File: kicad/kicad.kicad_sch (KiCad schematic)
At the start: 256 parts, among them J1 USB_B_Micro, J2 SWD, J3 pwr_led+, J4 pwr_led-, J5 caps_led+, J6 caps_led-, U1 AMS1117-3.3, Y1 16MGz, sw1 Esc, sw10 Z, sw100 N5, sw101 N6, sw102 N2, sw103 N1, sw104 N0, sw105 MPlay, sw106 MFwd, sw107 NSlash, sw108 NStar, sw109 N8, sw11 LCtrl, sw110 N9, sw111 NMinus, sw112 NPlus, sw113 NEnter, sw114 N3, sw115 NPeriod, sw12 LSys, sw13 F2, sw14 F3, sw15 2, sw16 3, sw17 W, sw18 E, sw19 S, sw2 F1, sw20 D, sw21 X, sw22 C, sw23 LAlt, sw24 THome, sw25 F4, sw26 F5, sw27 4, sw28 5, sw29 R, sw3 Tilda, sw30 T, sw31 F, sw32 G, sw33 V, sw34 B, sw35 LSpace, sw36 TLeft, sw37 F6, sw38 F7, sw39 6, sw4 1, sw40 7, sw41 Y, sw42 U, sw43 H, sw44 J, sw45 N, sw46 M, sw47 TUp, sw48 TDown, sw49 F8, sw5 Tab, sw50 F9, sw51 8, sw52 9, sw53 I, sw54 O, sw55 K, sw56 L, sw57 Comma, sw58 Period, sw59 RSpace, sw6 Q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

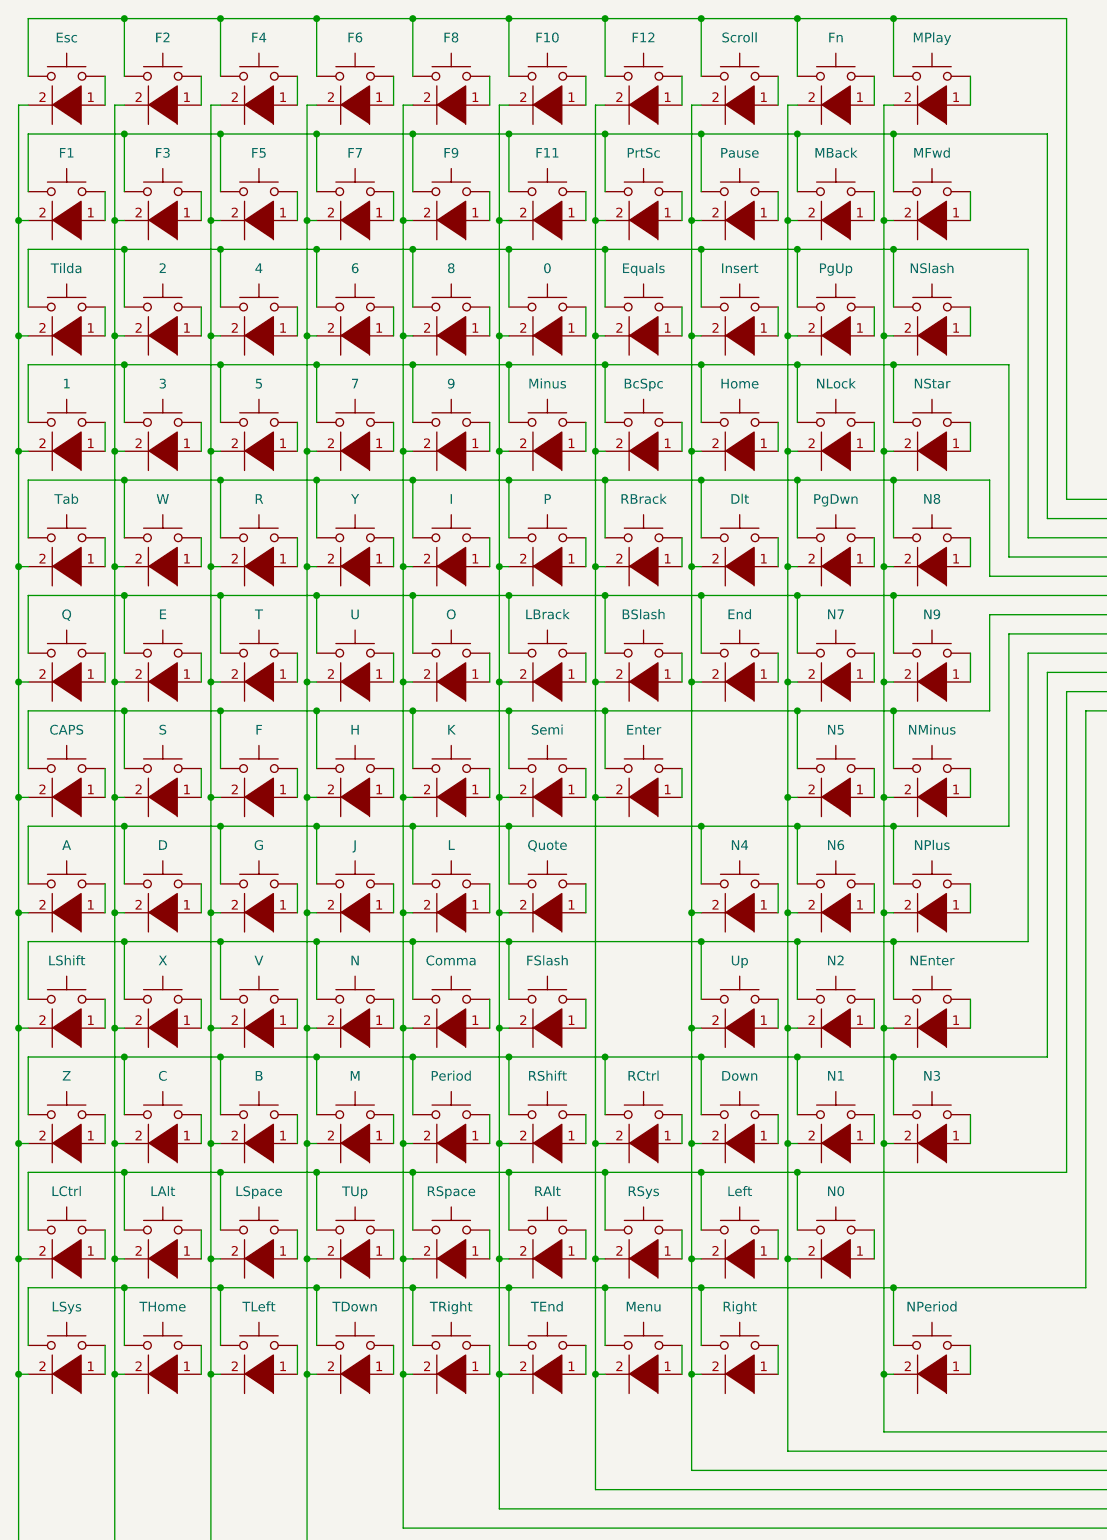
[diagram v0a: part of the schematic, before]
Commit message: layout new diodes
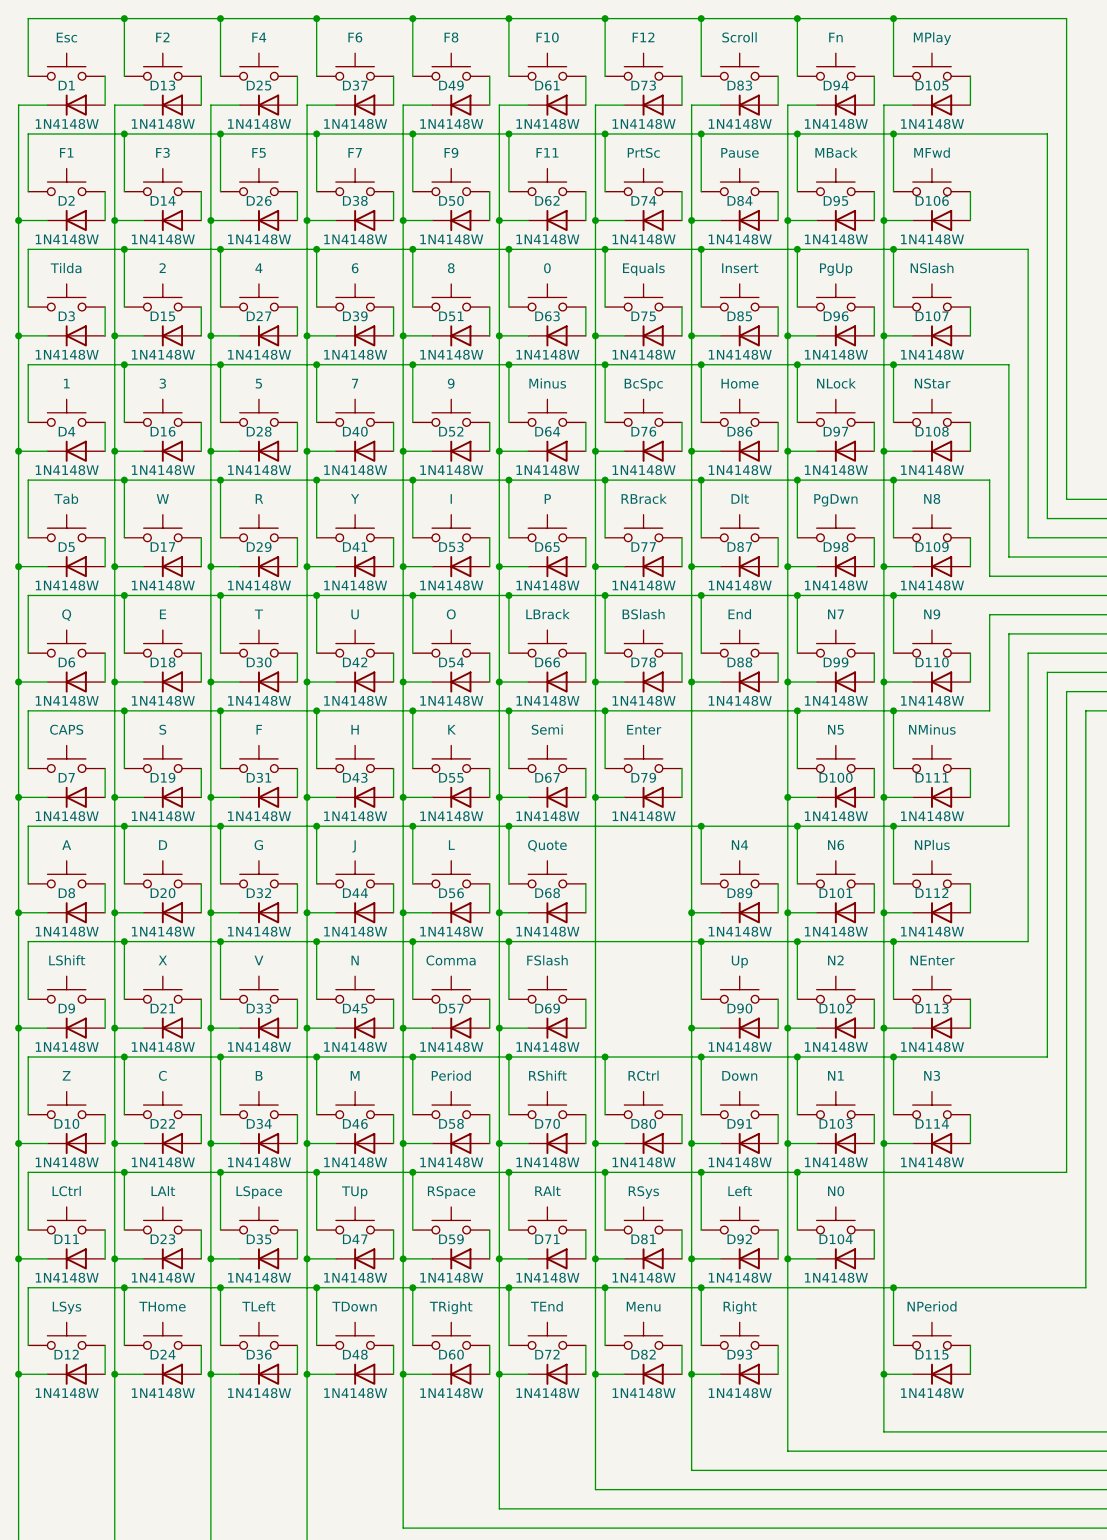
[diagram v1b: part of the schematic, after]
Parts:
- removed D1: D-Esc, Diode_SMD:D_SOD-123F, symbol pspice:DIODE
- removed D10: D-Z, Diode_SMD:D_SOD-123F, symbol pspice:DIODE
- removed D100: D-Num5, Diode_SMD:D_SOD-123F, symbol pspice:DIODE
- removed D101: D-Num6, Diode_SMD:D_SOD-123F, symbol pspice:DIODE
- removed D102: D-Num2, Diode_SMD:D_SOD-123F, symbol pspice:DIODE
- removed D103: D-Num1, Diode_SMD:D_SOD-123F, symbol pspice:DIODE
- removed D104: D-Num0, Diode_SMD:D_SOD-123F, symbol pspice:DIODE
- removed D105: D-mPlay, Diode_SMD:D_SOD-123F, symbol pspice:DIODE
- removed D106: D-mFwd, Diode_SMD:D_SOD-123F, symbol pspice:DIODE
- removed D107: D-Num/, Diode_SMD:D_SOD-123F, symbol pspice:DIODE
- removed D108: D-Num*, Diode_SMD:D_SOD-123F, symbol pspice:DIODE
- removed D109: D-Num8, Diode_SMD:D_SOD-123F, symbol pspice:DIODE
- removed D11: D-LCtrl, Diode_SMD:D_SOD-123F, symbol pspice:DIODE
- removed D110, D99: D-Num9, Diode_SMD:D_SOD-123F, symbol pspice:DIODE
- removed D111: D-Num-, Diode_SMD:D_SOD-123F, symbol pspice:DIODE
- removed D112: D-Num+, Diode_SMD:D_SOD-123F, symbol pspice:DIODE
- removed D113: D-NumEnter, Diode_SMD:D_SOD-123F, symbol pspice:DIODE
- removed D114: D-Num3, Diode_SMD:D_SOD-123F, symbol pspice:DIODE
- removed D115: D-Num., Diode_SMD:D_SOD-123F, symbol pspice:DIODE
- removed D12: D-LSys, Diode_SMD:D_SOD-123F, symbol pspice:DIODE
- removed D13: D-F2, Diode_SMD:D_SOD-123F, symbol pspice:DIODE
- removed D14: D-F3, Diode_SMD:D_SOD-123F, symbol pspice:DIODE
- removed D15: D-2, Diode_SMD:D_SOD-123F, symbol pspice:DIODE
- removed D16: D-3, Diode_SMD:D_SOD-123F, symbol pspice:DIODE
- removed D17: D-W, Diode_SMD:D_SOD-123F, symbol pspice:DIODE
- removed D18: D-E, Diode_SMD:D_SOD-123F, symbol pspice:DIODE
- removed D19: D-S, Diode_SMD:D_SOD-123F, symbol pspice:DIODE
- removed D2: D-F1, Diode_SMD:D_SOD-123F, symbol pspice:DIODE
- removed D20: D-D, Diode_SMD:D_SOD-123F, symbol pspice:DIODE
- removed D21: D-X, Diode_SMD:D_SOD-123F, symbol pspice:DIODE
- removed D22: D-C, Diode_SMD:D_SOD-123F, symbol pspice:DIODE
- removed D23: D-LAlt, Diode_SMD:D_SOD-123F, symbol pspice:DIODE
- removed D24: D-THome, Diode_SMD:D_SOD-123F, symbol pspice:DIODE
- removed D25: D-F4, Diode_SMD:D_SOD-123F, symbol pspice:DIODE
- removed D26: D-F5, Diode_SMD:D_SOD-123F, symbol pspice:DIODE
- removed D27: D-4, Diode_SMD:D_SOD-123F, symbol pspice:DIODE
- removed D28: D-5, Diode_SMD:D_SOD-123F, symbol pspice:DIODE
- removed D29: D-R, Diode_SMD:D_SOD-123F, symbol pspice:DIODE
- removed D3: D-Tilda, Diode_SMD:D_SOD-123F, symbol pspice:DIODE
- removed D30: D-T, Diode_SMD:D_SOD-123F, symbol pspice:DIODE
- removed D31: D-F, Diode_SMD:D_SOD-123F, symbol pspice:DIODE
- removed D32: D-G, Diode_SMD:D_SOD-123F, symbol pspice:DIODE
- removed D33: D-V, Diode_SMD:D_SOD-123F, symbol pspice:DIODE
- removed D34: D-B, Diode_SMD:D_SOD-123F, symbol pspice:DIODE
- removed D35: D-LSpace, Diode_SMD:D_SOD-123F, symbol pspice:DIODE
- removed D36: D-TLeft, Diode_SMD:D_SOD-123F, symbol pspice:DIODE
- removed D37: D-F6, Diode_SMD:D_SOD-123F, symbol pspice:DIODE
- removed D38: D-F7, Diode_SMD:D_SOD-123F, symbol pspice:DIODE
- removed D39: D-6, Diode_SMD:D_SOD-123F, symbol pspice:DIODE
- removed D4: D-1, Diode_SMD:D_SOD-123F, symbol pspice:DIODE
- removed D40: D-7, Diode_SMD:D_SOD-123F, symbol pspice:DIODE
- removed D41: D-Y, Diode_SMD:D_SOD-123F, symbol pspice:DIODE
- removed D42: D-U, Diode_SMD:D_SOD-123F, symbol pspice:DIODE
- removed D43: D-H, Diode_SMD:D_SOD-123F, symbol pspice:DIODE
- removed D44: D-J, Diode_SMD:D_SOD-123F, symbol pspice:DIODE
- removed D45: D-N, Diode_SMD:D_SOD-123F, symbol pspice:DIODE
- removed D46: D-M, Diode_SMD:D_SOD-123F, symbol pspice:DIODE
- removed D47: D-TUp, Diode_SMD:D_SOD-123F, symbol pspice:DIODE
- removed D48: D-TDown, Diode_SMD:D_SOD-123F, symbol pspice:DIODE
- removed D49: D-F8, Diode_SMD:D_SOD-123F, symbol pspice:DIODE
- removed D5: D-Tab, Diode_SMD:D_SOD-123F, symbol pspice:DIODE
- removed D50: D-F9, Diode_SMD:D_SOD-123F, symbol pspice:DIODE
- removed D51: D-8, Diode_SMD:D_SOD-123F, symbol pspice:DIODE
- removed D52: D-9, Diode_SMD:D_SOD-123F, symbol pspice:DIODE
- removed D53: D-I, Diode_SMD:D_SOD-123F, symbol pspice:DIODE
- removed D54: D-O, Diode_SMD:D_SOD-123F, symbol pspice:DIODE
- removed D55: D-K, Diode_SMD:D_SOD-123F, symbol pspice:DIODE
- removed D56: D-L, Diode_SMD:D_SOD-123F, symbol pspice:DIODE
- removed D57: D-,, Diode_SMD:D_SOD-123F, symbol pspice:DIODE
- removed D58: D-., Diode_SMD:D_SOD-123F, symbol pspice:DIODE
- removed D59: D-RSpace, Diode_SMD:D_SOD-123F, symbol pspice:DIODE
- removed D6: D-Q, Diode_SMD:D_SOD-123F, symbol pspice:DIODE
- removed D60: D-TRight, Diode_SMD:D_SOD-123F, symbol pspice:DIODE
- removed D61: D-F10, Diode_SMD:D_SOD-123F, symbol pspice:DIODE
- removed D62: D-F11, Diode_SMD:D_SOD-123F, symbol pspice:DIODE
- removed D63: D-0, Diode_SMD:D_SOD-123F, symbol pspice:DIODE
- removed D64: D--, Diode_SMD:D_SOD-123F, symbol pspice:DIODE
- removed D65: D-P, Diode_SMD:D_SOD-123F, symbol pspice:DIODE
- removed D66: D-[, Diode_SMD:D_SOD-123F, symbol pspice:DIODE
- removed D67: D-;, Diode_SMD:D_SOD-123F, symbol pspice:DIODE
- removed D68: D-', Diode_SMD:D_SOD-123F, symbol pspice:DIODE
- removed D69: D-/, Diode_SMD:D_SOD-123F, symbol pspice:DIODE
- removed D7: D-CAPS, Diode_SMD:D_SOD-123F, symbol pspice:DIODE
- removed D70: D-RShift, Diode_SMD:D_SOD-123F, symbol pspice:DIODE
- removed D71: D-RAlt, Diode_SMD:D_SOD-123F, symbol pspice:DIODE
- removed D72: D-TEnd, Diode_SMD:D_SOD-123F, symbol pspice:DIODE
- removed D73: D-F12, Diode_SMD:D_SOD-123F, symbol pspice:DIODE
- removed D74: D-PrtSc, Diode_SMD:D_SOD-123F, symbol pspice:DIODE
- removed D75: D-=, Diode_SMD:D_SOD-123F, symbol pspice:DIODE
- removed D76: D-BcSpc, Diode_SMD:D_SOD-123F, symbol pspice:DIODE
- removed D77: D-], Diode_SMD:D_SOD-123F, symbol pspice:DIODE
- removed D78: D-\, Diode_SMD:D_SOD-123F, symbol pspice:DIODE
- removed D79: D-Enter, Diode_SMD:D_SOD-123F, symbol pspice:DIODE
- removed D8: D-A, Diode_SMD:D_SOD-123F, symbol pspice:DIODE
- removed D80: D-RCtrl, Diode_SMD:D_SOD-123F, symbol pspice:DIODE
- removed D81: D-RSys, Diode_SMD:D_SOD-123F, symbol pspice:DIODE
- removed D82: D-Menu, Diode_SMD:D_SOD-123F, symbol pspice:DIODE
- removed D83: D-ScrLck, Diode_SMD:D_SOD-123F, symbol pspice:DIODE
- removed D84: D-Pause, Diode_SMD:D_SOD-123F, symbol pspice:DIODE
- removed D85: D-Insert, Diode_SMD:D_SOD-123F, symbol pspice:DIODE
- removed D86: D-Home, Diode_SMD:D_SOD-123F, symbol pspice:DIODE
- removed D87: D-Dlt, Diode_SMD:D_SOD-123F, symbol pspice:DIODE
- removed D88: D-End, Diode_SMD:D_SOD-123F, symbol pspice:DIODE
- removed D89: D-Num4, Diode_SMD:D_SOD-123F, symbol pspice:DIODE
- removed D9: D-LShift, Diode_SMD:D_SOD-123F, symbol pspice:DIODE
- removed D90: D-Up, Diode_SMD:D_SOD-123F, symbol pspice:DIODE
- removed D91: D-Down, Diode_SMD:D_SOD-123F, symbol pspice:DIODE
- removed D92: D-Left, Diode_SMD:D_SOD-123F, symbol pspice:DIODE
- removed D93: D-Right, Diode_SMD:D_SOD-123F, symbol pspice:DIODE
- removed D94: D-FN, Diode_SMD:D_SOD-123F, symbol pspice:DIODE
- removed D95: D-mBack, Diode_SMD:D_SOD-123F, symbol pspice:DIODE
- removed D96: D-PgUp, Diode_SMD:D_SOD-123F, symbol pspice:DIODE
- removed D97: D-NumLck, Diode_SMD:D_SOD-123F, symbol pspice:DIODE
- removed D98: D-PgDwn, Diode_SMD:D_SOD-123F, symbol pspice:DIODE
- added D1, D10, D100, D101, D102, D103, D104, D105, D106, D107, D108, D109, D11, D110, D111, D112, D113, D114, D115, D12, D13, D14, D15, D16, D17, D18, D19, D2, D20, D21, D22, D23, D24, D25, D26, D27, D28, D29, D3, D30, D31, D32, D33, D34, D35, D36, D37, D38, D39, D4, D40, D41, D42, D43, D44, D45, D46, D47, D48, D49, D5, D50, D51, D52, D53, D54, D55, D56, D57, D58, D59, D6, D60, D61, D62, D63, D64, D65, D66, D67, D68, D69, D7, D70, D71, D72, D73, D74, D75, D76, D77, D78, D79, D8, D80, D81, D82, D83, D84, D85, D86, D87, D88, D89, D9, D90, D91, D92, D93, D94, D95, D96, D97, D98, D99: 1N4148W, Diode_SMD:D_SOD-123, symbol Diode:1N4148W
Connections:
- net COLUMN1: now also D105.1 (K), D106.1 (K), D107.1 (K), D108.1 (K), D109.1 (K), D110.1 (K), D111.1 (K), D112.1 (K), D113.1 (K), D114.1 (K), D115.1 (K)
- net COLUMN10: now also D1.1 (K), D10.1 (K), D11.1 (K), D12.1 (K), D2.1 (K), D3.1 (K), D4.1 (K), D5.1 (K), D6.1 (K), D7.1 (K), D8.1 (K), D9.1 (K)
- net COLUMN2: now also D100.1 (K), D101.1 (K), D102.1 (K), D103.1 (K), D104.1 (K), D94.1 (K), D95.1 (K), D96.1 (K), D97.1 (K), D98.1 (K), D99.1 (K)
- net COLUMN3: now also D83.1 (K), D84.1 (K), D85.1 (K), D86.1 (K), D87.1 (K), D88.1 (K), D89.1 (K), D90.1 (K), D91.1 (K), D92.1 (K), D93.1 (K)
- net COLUMN4: now also D73.1 (K), D74.1 (K), D75.1 (K), D76.1 (K), D77.1 (K), D78.1 (K), D79.1 (K), D80.1 (K), D81.1 (K), D82.1 (K)
- net COLUMN5: now also D61.1 (K), D62.1 (K), D63.1 (K), D64.1 (K), D65.1 (K), D66.1 (K), D67.1 (K), D68.1 (K), D69.1 (K), D70.1 (K), D71.1 (K), D72.1 (K)
- net COLUMN6: now also D49.1 (K), D50.1 (K), D51.1 (K), D52.1 (K), D53.1 (K), D54.1 (K), D55.1 (K), D56.1 (K), D57.1 (K), D58.1 (K), D59.1 (K), D60.1 (K)
- net COLUMN7: now also D37.1 (K), D38.1 (K), D39.1 (K), D40.1 (K), D41.1 (K), D42.1 (K), D43.1 (K), D44.1 (K), D45.1 (K), D46.1 (K), D47.1 (K), D48.1 (K)
- net COLUMN8: now also D25.1 (K), D26.1 (K), D27.1 (K), D28.1 (K), D29.1 (K), D30.1 (K), D31.1 (K), D32.1 (K), D33.1 (K), D34.1 (K), D35.1 (K), D36.1 (K)
- net COLUMN9: now also D13.1 (K), D14.1 (K), D15.1 (K), D16.1 (K), D17.1 (K), D18.1 (K), D19.1 (K), D20.1 (K), D21.1 (K), D22.1 (K), D23.1 (K), D24.1 (K)
- net at sw17.2: now also D17.2 (A)
- net at sw104.2: now also D104.2 (A)
- net at sw38.2: now also D38.2 (A)
- net at sw59.2: now also D59.2 (A)
- net at sw1.2: now also D1.2 (A)
- net at sw19.2: now also D19.2 (A)
- net at sw70.2: now also D70.2 (A)
- net at sw102.2: now also D102.2 (A)
- net at sw47.2: now also D47.2 (A)
- net at sw92.2: now also D92.2 (A)
- net at sw48.2: now also D48.2 (A)
- net at sw72.2: now also D72.2 (A)
- net at sw34.2: now also D34.2 (A)
- net at sw40.2: now also D40.2 (A)
- net at sw99.2: now also D99.2 (A)
- net at sw24.2: now also D24.2 (A)
- net at sw12.2: now also D12.2 (A)
- net at sw80.2: now also D80.2 (A)
- net at sw113.2: now also D113.2 (A)
- net at sw91.2: now also D91.2 (A)
- net at sw63.2: now also D63.2 (A)
- net at sw100.2: now also D100.2 (A)
- net at sw36.2: now also D36.2 (A)
- net at sw53.2: now also D53.2 (A)
- net at sw106.2: now also D106.2 (A)
- net at sw27.2: now also D27.2 (A)
- net at sw60.2: now also D60.2 (A)
- net at sw8.2: now also D8.2 (A)
- net at sw9.2: now also D9.2 (A)
- net at sw58.2: now also D58.2 (A)
- net at sw98.2: now also D98.2 (A)
- net at sw51.2: now also D51.2 (A)
- net at sw7.2: now also D7.2 (A)
- net at sw20.2: now also D20.2 (A)
- net at sw22.2: now also D22.2 (A)
- net at sw28.2: now also D28.2 (A)
- net at sw35.2: now also D35.2 (A)
- net at sw84.2: now also D84.2 (A)
- net at sw13.2: now also D13.2 (A)
- net at sw97.2: now also D97.2 (A)
- net at sw71.2: now also D71.2 (A)
- net at sw61.2: now also D61.2 (A)
- net at sw50.2: now also D50.2 (A)
- net at sw86.2: now also D86.2 (A)
- net at sw109.2: now also D109.2 (A)
- net at sw41.2: now also D41.2 (A)
- net at sw85.2: now also D85.2 (A)
- net at sw31.2: now also D31.2 (A)
- net at sw93.2: now also D93.2 (A)
- net at sw16.2: now also D16.2 (A)
- net at sw75.2: now also D75.2 (A)
- net at sw78.2: now also D78.2 (A)
- net at sw26.2: now also D26.2 (A)
- net at sw21.2: now also D21.2 (A)
- net at sw89.2: now also D89.2 (A)
- net at sw74.2: now also D74.2 (A)
- net at sw25.2: now also D25.2 (A)
- net at sw103.2: now also D103.2 (A)
- net at sw114.2: now also D114.2 (A)
- net at sw29.2: now also D29.2 (A)
- net at sw14.2: now also D14.2 (A)
- net at sw73.2: now also D73.2 (A)
- net at sw105.2: now also D105.2 (A)
- net at sw6.2: now also D6.2 (A)
- net at sw55.2: now also D55.2 (A)
- net at sw67.2: now also D67.2 (A)
- net at sw87.2: now also D87.2 (A)
- net at sw69.2: now also D69.2 (A)
- net at sw45.2: now also D45.2 (A)
- net at sw54.2: now also D54.2 (A)
- net at sw77.2: now also D77.2 (A)
- net at sw23.2: now also D23.2 (A)
- net at sw79.2: now also D79.2 (A)
- net at sw66.2: now also D66.2 (A)
- net at sw18.2: now also D18.2 (A)
- net at sw64.2: now also D64.2 (A)
- net at sw52.2: now also D52.2 (A)
- net at sw96.2: now also D96.2 (A)
- net at sw10.2: now also D10.2 (A)
- net at sw111.2: now also D111.2 (A)
- net at sw5.2: now also D5.2 (A)
- net at sw46.2: now also D46.2 (A)
- net at sw4.2: now also D4.2 (A)
- net at sw107.2: now also D107.2 (A)
- net at sw62.2: now also D62.2 (A)
- net at sw88.2: now also D88.2 (A)
- net at sw33.2: now also D33.2 (A)
- net at sw43.2: now also D43.2 (A)
- net at sw108.2: now also D108.2 (A)
- net at sw90.2: now also D90.2 (A)
- net at sw112.2: now also D112.2 (A)
- net at sw95.2: now also D95.2 (A)
- net at sw68.2: now also D68.2 (A)
- net at sw76.2: now also D76.2 (A)
- net at sw94.2: now also D94.2 (A)
- net at sw44.2: now also D44.2 (A)
- net at sw49.2: now also D49.2 (A)
- net at sw115.2: now also D115.2 (A)
- net at sw30.2: now also D30.2 (A)
- net at sw2.2: now also D2.2 (A)
- net at sw42.2: now also D42.2 (A)
- net at sw39.2: now also D39.2 (A)
- net at sw82.2: now also D82.2 (A)
- net at sw56.2: now also D56.2 (A)
- net at sw37.2: now also D37.2 (A)
- net at sw81.2: now also D81.2 (A)
- net at sw65.2: now also D65.2 (A)
- net at sw15.2: now also D15.2 (A)
- net at sw11.2: now also D11.2 (A)
- net at sw57.2: now also D57.2 (A)
- net at sw3.2: now also D3.2 (A)
- net at sw101.2: now also D101.2 (A)
- net at sw110.2: now also D110.2 (A)
- net at sw83.2: now also D83.2 (A)
- net at sw32.2: now also D32.2 (A)

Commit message: correct RShift footprint
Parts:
- sw70: footprint Button_Switch_Keyboard:SW_Cherry_MX_1.00u_PCB -> Button_Switch_Keyboard:SW_Cherry_MX_2.75u_PCB
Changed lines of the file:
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@@
     )
     (property "Value" "RShift" (id 1) (at 105.41 172.72 0))
-    (property "Footprint" "Button_Switch_Keyboard:SW_Cherry_MX_1.00u_PCB" (id 2) (at 105.41 172.72 0)
+    (property "Footprint" "Button_Switch_Keyboard:SW_Cherry_MX_2.75u_PCB" (id 2) (at 105.41 172.72 0)
       (effects (font (size 1.27 1.27)) hide)
     )
@@
     )
     (path "/0a2fbe5c-c0e6-4b3a-854e-12d87ec302d2"
-      (reference "sw70") (unit 1) (value "RShift") (footprint "Button_Switch_Keyboard:SW_Cherry_MX_1.00u_PCB")
+      (reference "sw70") (unit 1) (value "RShift") (footprint "Button_Switch_Keyboard:SW_Cherry_MX_2.75u_PCB")
     )
     (path "/35cfa04a-c5c4-4d67-bfb5-7569bc2b66f1"

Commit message: 75% layout
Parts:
- removed D100, D101, D102, D103, D104, D105, D106, D107, D108, D109, D110, D111, D112, D113, D114, D115, D83, D84, D86, D88, D89, D90, D91, D92, D93, D94, D95, D97, D99: 1N4148W, Diode_SMD:D_SOD-123, symbol Diode:1N4148W
- removed sw100: N5, Button_Switch_Keyboard:SW_Cherry_MX_1.00u_PCB, symbol Switch:SW_Push
- removed sw101: N6, Button_Switch_Keyboard:SW_Cherry_MX_1.00u_PCB, symbol Switch:SW_Push
- removed sw102: N2, Button_Switch_Keyboard:SW_Cherry_MX_1.00u_PCB, symbol Switch:SW_Push
- removed sw103: N1, Button_Switch_Keyboard:SW_Cherry_MX_1.00u_PCB, symbol Switch:SW_Push
- removed sw104: N0, Button_Switch_Keyboard:SW_Cherry_MX_2.00u_PCB, symbol Switch:SW_Push
- removed sw105: MPlay, Button_Switch_Keyboard:SW_Cherry_MX_1.00u_PCB, symbol Switch:SW_Push
- removed sw106: MFwd, Button_Switch_Keyboard:SW_Cherry_MX_1.00u_PCB, symbol Switch:SW_Push
- removed sw107: NSlash, Button_Switch_Keyboard:SW_Cherry_MX_1.00u_PCB, symbol Switch:SW_Push
- removed sw108: NStar, Button_Switch_Keyboard:SW_Cherry_MX_1.00u_PCB, symbol Switch:SW_Push
- removed sw109: N8, Button_Switch_Keyboard:SW_Cherry_MX_1.00u_PCB, symbol Switch:SW_Push
- removed sw110: N9, Button_Switch_Keyboard:SW_Cherry_MX_1.00u_PCB, symbol Switch:SW_Push
- removed sw111: NMinus, Button_Switch_Keyboard:SW_Cherry_MX_1.00u_PCB, symbol Switch:SW_Push
- removed sw112: NPlus, Button_Switch_Keyboard:SW_Cherry_MX_2.00u_Vertical_PCB, symbol Switch:SW_Push
- removed sw113: NEnter, Button_Switch_Keyboard:SW_Cherry_MX_2.00u_Vertical_PCB, symbol Switch:SW_Push
- removed sw114: N3, Button_Switch_Keyboard:SW_Cherry_MX_1.00u_PCB, symbol Switch:SW_Push
- removed sw115: NPeriod, Button_Switch_Keyboard:SW_Cherry_MX_1.00u_PCB, symbol Switch:SW_Push
- removed sw83: Scroll, Button_Switch_Keyboard:SW_Cherry_MX_1.00u_PCB, symbol Switch:SW_Push
- removed sw84: Pause, Button_Switch_Keyboard:SW_Cherry_MX_1.00u_PCB, symbol Switch:SW_Push
- removed sw86: Home, Button_Switch_Keyboard:SW_Cherry_MX_1.00u_PCB, symbol Switch:SW_Push
- removed sw88: End, Button_Switch_Keyboard:SW_Cherry_MX_1.00u_PCB, symbol Switch:SW_Push
- removed sw89: N4, Button_Switch_Keyboard:SW_Cherry_MX_1.00u_PCB, symbol Switch:SW_Push
- removed sw90: Up, Button_Switch_Keyboard:SW_Cherry_MX_1.00u_PCB, symbol Switch:SW_Push
- removed sw91: Down, Button_Switch_Keyboard:SW_Cherry_MX_1.00u_PCB, symbol Switch:SW_Push
- removed sw92: Left, Button_Switch_Keyboard:SW_Cherry_MX_1.00u_PCB, symbol Switch:SW_Push
- removed sw93: Right, Button_Switch_Keyboard:SW_Cherry_MX_1.00u_PCB, symbol Switch:SW_Push
- removed sw94: Fn, Button_Switch_Keyboard:SW_Cherry_MX_1.00u_PCB, symbol Switch:SW_Push
- removed sw95: MBack, Button_Switch_Keyboard:SW_Cherry_MX_1.00u_PCB, symbol Switch:SW_Push
- removed sw97: NLock, Button_Switch_Keyboard:SW_Cherry_MX_1.00u_PCB, symbol Switch:SW_Push
- removed sw99: N7, Button_Switch_Keyboard:SW_Cherry_MX_1.00u_PCB, symbol Switch:SW_Push
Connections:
- net COLUMN1: now also D1.1 (K), D11.1 (K), D3.1 (K), D5.1 (K), D7.1 (K), D9.1 (K)
- net COLUMN10: now also D49.1 (K), D52.1 (K), D54.1 (K), D56.1 (K), D58.1 (K), D71.1 (K); no longer D1.1 (K), D10.1 (K), D11.1 (K), D12.1 (K), D2.1 (K), D3.1 (K), D4.1 (K), D5.1 (K), D6.1 (K), D7.1 (K), D8.1 (K), D9.1 (K)
- net COLUMN2: now also MCU1.39 (PC8), sw15.1, sw16.1, sw27.1, sw28.1, sw3.1, sw39.1, sw4.1, sw40.1, sw51.1, sw52.1, sw63.1, sw64.1, sw75.1, sw76.1; no longer D96.1 (K), D98.1 (K)
- net COLUMN3: now also D15.1 (K), D17.1 (K), D19.1 (K), D2.1 (K), D21.1 (K), D23.1 (K), D96.1 (K); no longer D85.1 (K), D87.1 (K)
- net COLUMN4: now also D13.1 (K), D16.1 (K), D18.1 (K), D20.1 (K), D22.1 (K), D24.1 (K), D35.1 (K); no longer D73.1 (K), D74.1 (K), D75.1 (K), D76.1 (K), D77.1 (K), D78.1 (K), D79.1 (K), D80.1 (K), D81.1 (K), D82.1 (K)
- net COLUMN5: now also D14.1 (K), D27.1 (K), D29.1 (K), D31.1 (K), D33.1 (K), D36.1 (K); no longer D61.1 (K), D62.1 (K), D63.1 (K), D64.1 (K), D65.1 (K), D66.1 (K), D67.1 (K), D68.1 (K), D69.1 (K), D70.1 (K), D71.1 (K), D72.1 (K)
- net COLUMN6: now also D25.1 (K), D28.1 (K), D30.1 (K), D32.1 (K), D34.1 (K), D47.1 (K), D48.1 (K); no longer D49.1 (K), D50.1 (K), D51.1 (K), D52.1 (K), D53.1 (K), D54.1 (K), D55.1 (K), D56.1 (K), D57.1 (K), D58.1 (K), D59.1 (K), D60.1 (K)
- net COLUMN7: now also D26.1 (K), D60.1 (K); no longer D37.1 (K), D38.1 (K), D40.1 (K), D42.1 (K), D44.1 (K), D46.1 (K), D47.1 (K), D48.1 (K)
- net COLUMN8: now also D37.1 (K), D40.1 (K), D42.1 (K), D44.1 (K), D46.1 (K), D59.1 (K), D72.1 (K); no longer D25.1 (K), D26.1 (K), D27.1 (K), D28.1 (K), D29.1 (K), D30.1 (K), D31.1 (K), D32.1 (K), D33.1 (K), D34.1 (K), D35.1 (K), D36.1 (K)
- net COLUMN9: now also D38.1 (K), D51.1 (K), D53.1 (K), D55.1 (K), D57.1 (K), D98.1 (K); no longer D13.1 (K), D14.1 (K), D15.1 (K), D16.1 (K), D17.1 (K), D18.1 (K), D19.1 (K), D20.1 (K), D21.1 (K), D22.1 (K), D23.1 (K), D24.1 (K)
- net ROW1: now also sw2.1, sw26.1, sw38.1, sw50.1, sw62.1
- net ROW10: no longer sw10.1, sw22.1, sw34.1, sw46.1, sw58.1, sw70.1, sw80.1
- net ROW11: no longer sw11.1, sw23.1, sw35.1, sw47.1, sw59.1, sw71.1, sw81.1
- net ROW12: no longer sw12.1, sw24.1, sw36.1, sw48.1, sw60.1, sw72.1, sw82.1
- net ROW3: now also sw17.1, sw18.1, sw29.1, sw30.1, sw41.1, sw42.1, sw5.1, sw53.1, sw54.1, sw6.1, sw65.1, sw66.1, sw77.1, sw78.1; no longer sw15.1, sw27.1, sw3.1, sw39.1, sw51.1, sw63.1, sw75.1, sw85.1, sw96.1
- net ROW4: now also sw19.1, sw20.1, sw31.1, sw32.1, sw43.1, sw44.1, sw55.1, sw56.1, sw67.1, sw68.1, sw7.1, sw79.1, sw8.1, sw87.1; no longer sw16.1, sw28.1, sw4.1, sw40.1, sw52.1, sw64.1, sw76.1
- net ROW5: now also sw10.1, sw21.1, sw22.1, sw33.1, sw34.1, sw45.1, sw46.1, sw57.1, sw58.1, sw69.1, sw70.1, sw85.1, sw9.1; no longer sw17.1, sw29.1, sw41.1, sw5.1, sw53.1, sw65.1, sw77.1, sw87.1, sw98.1
- net ROW6: now also sw11.1, sw12.1, sw23.1, sw35.1, sw47.1, sw59.1, sw71.1, sw74.1, sw80.1, sw81.1, sw82.1; no longer sw18.1, sw30.1, sw42.1, sw54.1, sw6.1, sw66.1, sw78.1
- net ROW7: now also sw24.1, sw36.1, sw48.1, sw60.1, sw72.1, sw96.1, sw98.1; no longer sw19.1, sw31.1, sw43.1, sw55.1, sw67.1, sw7.1, sw79.1
- net ROW8: no longer sw20.1, sw32.1, sw44.1, sw56.1, sw68.1, sw8.1
- net ROW9: no longer sw21.1, sw33.1, sw45.1, sw57.1, sw69.1, sw9.1
- removed net ROW2: MCU1.39 (PC8), sw14.1, sw2.1, sw26.1, sw38.1, sw50.1, sw62.1, sw74.1
- new net: D10.1 (K), D12.1 (K), D4.1 (K), D6.1 (K), D8.1 (K)
- new net COLUMN11: D50.1 (K), D63.1 (K), D65.1 (K), D67.1 (K), D69.1 (K), D81.1 (K)
- new net COLUMN12: D61.1 (K), D64.1 (K), D66.1 (K), D68.1 (K), D82.1 (K)
- new net COLUMN13: D62.1 (K), D74.1 (K), D75.1 (K), D77.1 (K), D85.1 (K), D87.1 (K)
- new net COLUMN14: D70.1 (K), D73.1 (K), D76.1 (K), D78.1 (K), D79.1 (K), D80.1 (K)
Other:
- moved on the sheet: D1, D10, D11, D12, D13, D14, D15, D16, D17, D18, D19, D2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

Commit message: wip
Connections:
- net COLUMN2: now also D10.1 (K), D12.1 (K), D4.1 (K), D6.1 (K), D8.1 (K); no longer MCU1.39 (PC8), sw15.1, sw16.1, sw27.1, sw28.1, sw3.1, sw39.1, sw4.1, sw40.1, sw51.1, sw52.1, sw63.1, sw64.1, sw75.1, sw76.1
- net ROW1: now also sw14.1
- new net ROW2: MCU1.39 (PC8), sw15.1, sw16.1, sw27.1, sw28.1, sw3.1, sw39.1, sw4.1, sw40.1, sw51.1, sw52.1, sw63.1, sw64.1, sw75.1, sw76.1
